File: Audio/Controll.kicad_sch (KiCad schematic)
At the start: 5 parts, among them K1 AZ850-x, K2 AZ850-x

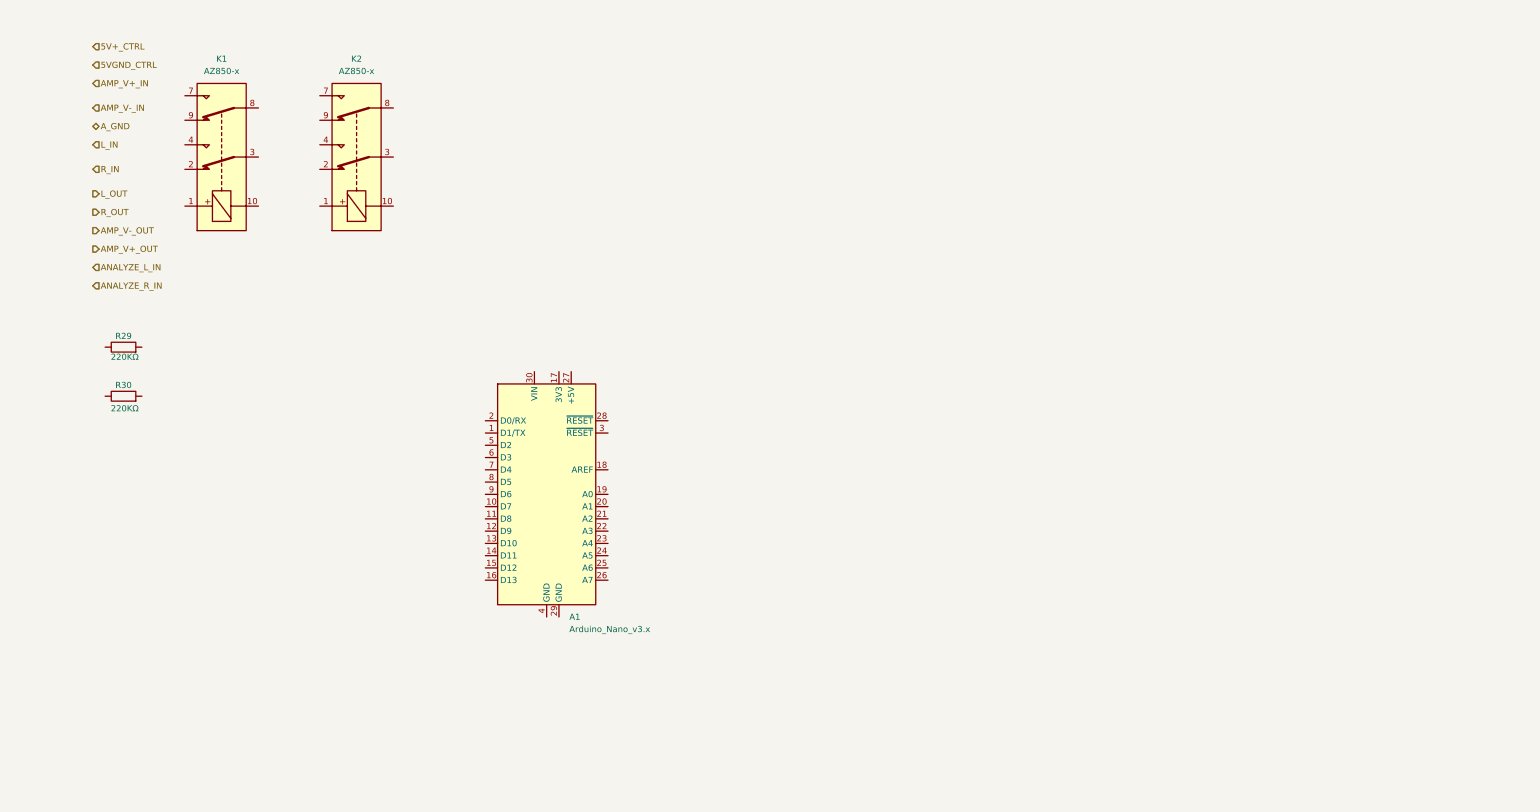
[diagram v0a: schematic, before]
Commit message: add relay
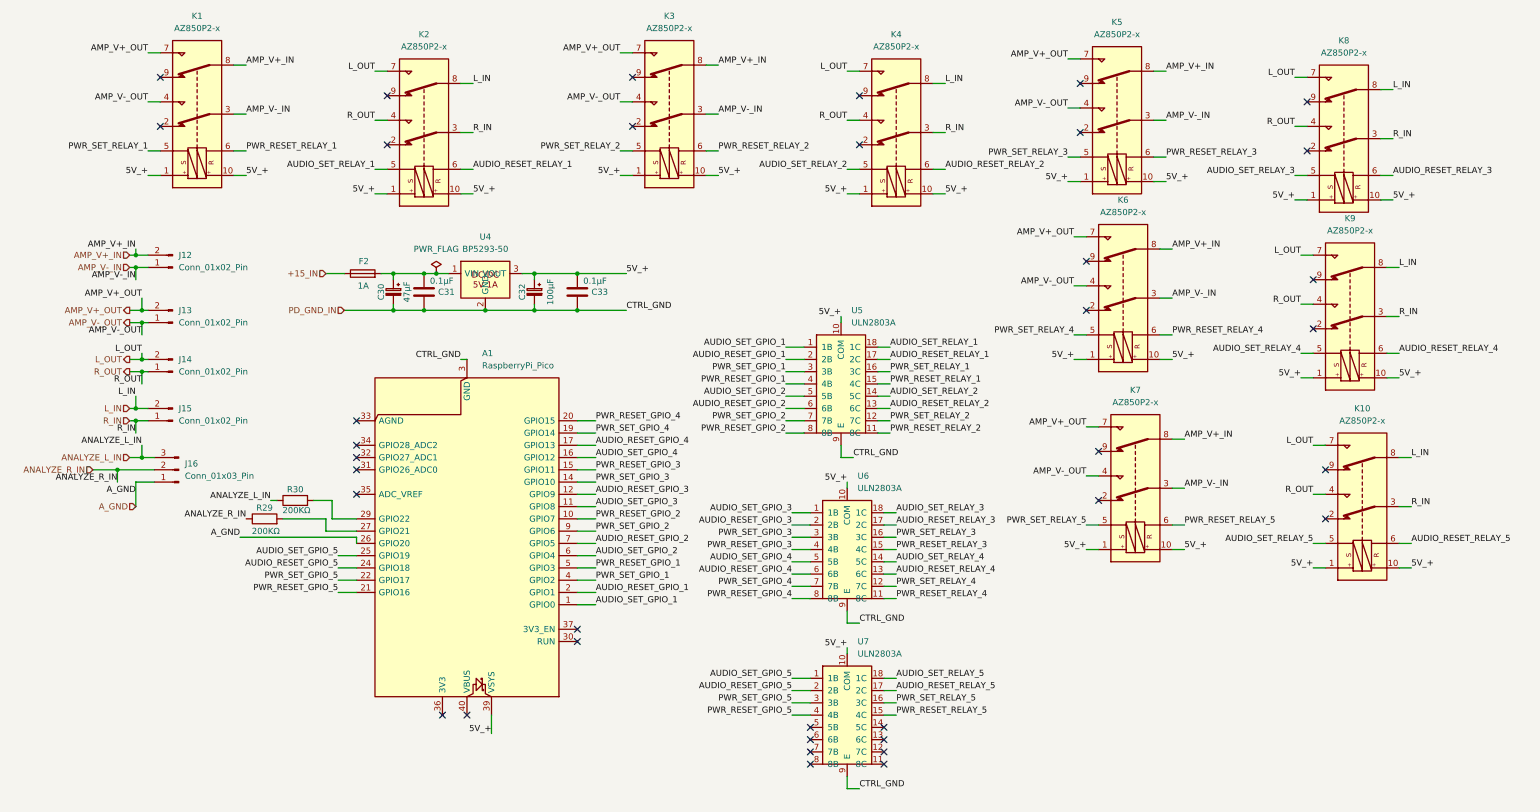
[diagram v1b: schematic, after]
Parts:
- removed A1: Arduino_Nano_v3.x, Module:Arduino_Nano, symbol MCU_Module:Arduino_Nano_v3.x
- removed K1, K2: AZ850-x, Relay_THT:Relay_DPDT_FRT5, symbol Relay:AZ850-x
- added A1: RaspberryPi_Pico, Module:RaspberryPi_Pico_Common_Unspecified, symbol MCU_Module:RaspberryPi_Pico
- added C30: 47μF, Capacitor_THT:CP_Radial_D8.0mm_P3.50mm, symbol Device:C_Polarized_Small
- added C31, C33: 0.1μF, Capacitor_THT:C_Disc_D5.0mm_W2.5mm_P2.50mm, symbol Device:C
- added C32: 100μF, Capacitor_THT:CP_Radial_D6.3mm_P2.50mm, symbol Device:C_Polarized_Small
- added F2: 1A, Resistor_THT:R_Axial_DIN0411_L9.9mm_D3.6mm_P12.70mm_Horizontal, symbol Device:Fuse
- added J12, J13, J14, J15: Conn_01x02_Pin, symbol Connector:Conn_01x02_Pin
- added J16: Conn_01x03_Pin, symbol Connector:Conn_01x03_Pin
- added K1, K10, K2, K3, K4, K5, K6, K7, K8, K9: AZ850P2-x, Relay_THT:Relay_DPDT_FRT5, symbol Relay:AZ850P2-x
- added U4: BP5293-50, BP5293_ROHM:BP5293-50_ROHM_SIP-3, symbol BP5293-50:BP5293-50
- added U5, U6, U7: ULN2803A, ULN2803A_HTC_DIP_ONLY:ULN2803A_DIP-18_W7.62mm, symbol ULN2803A:ULN2803A
- R29: renamed from R30; value 220KΩ -> 200KΩ
- R30: renamed from R29; value 220KΩ -> 200KΩ
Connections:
- net AMP_V+_IN: now also J12.2 (Pin_2), K1.8, K3.8, K5.8, K6.8, K7.8
- net AMP_V+_OUT: now also J13.2 (Pin_2), K1.7, K3.7, K5.7, K6.7, K7.7
- net AMP_V-_IN: now also J12.1 (Pin_1), K1.3, K3.3, K5.3, K6.3, K7.3
- net AMP_V-_OUT: now also J13.1 (Pin_1), K1.4, K3.4, K5.4, K6.4, K7.4
- net ANALYZE_L_IN: now also R30.1, J16.3 (Pin_3)
- net ANALYZE_R_IN: now also R29.1, J16.2 (Pin_2)
- net A_GND: now also A1.26 (GPIO20), J16.1 (Pin_1)
- net L_IN: now also J15.2 (Pin_2), K10.8, K2.8, K4.8, K8.8, K9.8
- net L_OUT: now also J14.2 (Pin_2), K10.7, K2.7, K4.7, K8.7, K9.7
- net R_IN: now also J15.1 (Pin_1), K10.3, K2.3, K4.3, K8.3, K9.3
- net R_OUT: now also J14.1 (Pin_1), K10.4, K2.4, K4.4, K8.4, K9.4
- net at R30.2: now also A1.29 (GPIO22)
- net at R29.2: now also A1.27 (GPIO21)
- new net: C30.1, C31.1, F2.2, U4.1 (VIN)
- new net +15_IN: F2.1
- new net 5V_+: A1.39 (VSYS), C32.1, C33.1, K1.1, K1.10, K10.1, K10.10, K2.1, K2.10, K3.1, K3.10, K4.1, K4.10, K5.1, K5.10, K6.1, K6.10, K7.1, K7.10, K8.1, K8.10, K9.1, K9.10, U4.3 (VOUT), U5.10 (COM), U6.10 (COM), U7.10 (COM)
- new net AUDIO_RESET_GPIO_1: A1.2 (GPIO1), U5.2 (2B)
- new net AUDIO_RESET_GPIO_2: A1.7 (GPIO5), U5.6 (6B)
- new net AUDIO_RESET_GPIO_3: A1.12 (GPIO9), U6.2 (2B)
- new net AUDIO_RESET_GPIO_4: A1.17 (GPIO13), U6.6 (6B)
- new net AUDIO_RESET_GPIO_5: A1.24 (GPIO18), U7.2 (2B)
- new net AUDIO_RESET_RELAY_1: K2.6, U5.17 (2C)
- new net AUDIO_RESET_RELAY_2: K4.6, U5.13 (6C)
- new net AUDIO_RESET_RELAY_3: K8.6, U6.17 (2C)
- new net AUDIO_RESET_RELAY_4: K9.6, U6.13 (6C)
- new net AUDIO_RESET_RELAY_5: K10.6, U7.17 (2C)
- new net AUDIO_SET_GPIO_1: A1.1 (GPIO0), U5.1 (1B)
- new net AUDIO_SET_GPIO_2: A1.6 (GPIO4), U5.5 (5B)
- new net AUDIO_SET_GPIO_3: A1.11 (GPIO8), U6.1 (1B)
- new net AUDIO_SET_GPIO_4: A1.16 (GPIO12), U6.5 (5B)
- new net AUDIO_SET_GPIO_5: A1.25 (GPIO19), U7.1 (1B)
- new net AUDIO_SET_RELAY_1: K2.5, U5.18 (1C)
- new net AUDIO_SET_RELAY_2: K4.5, U5.14 (5C)
- new net AUDIO_SET_RELAY_3: K8.5, U6.18 (1C)
- new net AUDIO_SET_RELAY_4: K9.5, U6.14 (5C)
- new net AUDIO_SET_RELAY_5: K10.5, U7.18 (1C)
- new net PD_GND_IN: A1.13 (GND), A1.18 (GND), A1.23 (GND), A1.28 (GND), A1.3 (GND), A1.38 (GND), A1.8 (GND), C30.2, C31.2, C32.2, C33.2, U4.2 (GND), U5.9 (E), U6.9 (E), U7.9 (E)
- new net PWR_RESET_GPIO_1: A1.5 (GPIO3), U5.4 (4B)
- new net PWR_RESET_GPIO_2: A1.10 (GPIO7), U5.8 (8B)
- new net PWR_RESET_GPIO_3: A1.15 (GPIO11), U6.4 (4B)
- new net PWR_RESET_GPIO_4: A1.20 (GPIO15), U6.8 (8B)
- new net PWR_RESET_GPIO_5: A1.21 (GPIO16), U7.4 (4B)
- new net PWR_RESET_RELAY_1: K1.6, U5.15 (4C)
- new net PWR_RESET_RELAY_2: K3.6, U5.11 (8C)
- new net PWR_RESET_RELAY_3: K5.6, U6.15 (4C)
- new net PWR_RESET_RELAY_4: K6.6, U6.11 (8C)
- new net PWR_RESET_RELAY_5: K7.6, U7.15 (4C)
- new net PWR_SET_GPIO_1: A1.4 (GPIO2), U5.3 (3B)
- new net PWR_SET_GPIO_2: A1.9 (GPIO6), U5.7 (7B)
- new net PWR_SET_GPIO_3: A1.14 (GPIO10), U6.3 (3B)
- new net PWR_SET_GPIO_4: A1.19 (GPIO14), U6.7 (7B)
- new net PWR_SET_GPIO_5: A1.22 (GPIO17), U7.3 (3B)
- new net PWR_SET_RELAY_1: K1.5, U5.16 (3C)
- new net PWR_SET_RELAY_2: K3.5, U5.12 (7C)
- new net PWR_SET_RELAY_3: K5.5, U6.16 (3C)
- new net PWR_SET_RELAY_4: K6.5, U6.12 (7C)
- new net PWR_SET_RELAY_5: K7.5, U7.16 (3C)
- no-connect marks 0 -> 37
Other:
- moved on the sheet: R29, R30

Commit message: remove analyze
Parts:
- removed J16: Conn_01x03_Pin, symbol Connector:Conn_01x03_Pin
- removed R29, R30: 200KΩ, Resistor_SMD:R_1206_3216Metric_Pad1.30x1.75mm_HandSolder, symbol Device:R
- added J17: Conn_01x02_Pin, symbol Connector:Conn_01x02_Pin
- added NT1: NetTie_2, symbol Device:NetTie_2
- U4: symbol BP5293-50:BP5293-50 -> BP5293_ROHM:BP5293-50
- U5, U6, U7: footprint ULN2803A_HTC_DIP_ONLY:ULN2803A_DIP-18_W7.62mm -> Library:ULN2803A_DIP-18_W7.62mm; symbol ULN2803A:ULN2803A -> Transistor_Array:ULN2803A
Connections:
- net +15_IN: now also J17.2 (Pin_2)
- net PD_GND_IN: now also J17.1 (Pin_1), NT1.1; no longer A1.13 (GND), A1.18 (GND), A1.23 (GND), A1.28 (GND), A1.3 (GND), A1.38 (GND), A1.8 (GND), C30.2, C31.2, C32.2, C33.2, U4.2 (GND), U5.9 (E), U6.9 (E), U7.9 (E)
- net A_GND: no longer names the net of A1.26 (GPIO20)
- new net CTRL_GND: A1.13 (GND), A1.18 (GND), A1.23 (GND), A1.28 (GND), A1.3 (GND), A1.38 (GND), A1.8 (GND), C30.2, C31.2, C32.2, C33.2, NT1.2, U4.2 (GND), U5.9 (GND), U6.9 (GND), U7.9 (GND)
- no-connect marks 37 -> 40

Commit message: connect gnd
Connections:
- net CTRL_GND: now also U7.5 (I5), U7.6 (I6), U7.7 (I7), U7.8 (I8)
- no-connect marks 40 -> 36
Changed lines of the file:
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@@
+	)
+	(junction
+		(at 162.56 168.91)
+		(diameter 0)
+		(color 0 0 0 0)
 	)
 	(junction
@@
 	)
 	(junction
+		(at 162.56 167.64)
+		(diameter 0)
+		(color 0 0 0 0)
+	)
+	(junction
 		(at 120.65 67.31)
 		(diameter 0)
@@
 	)
 	(junction
+		(at 162.56 166.37)
+		(diameter 0)
+		(color 0 0 0 0)
+	)
+	(junction
 		(at 27.94 128.27)
 		(diameter 0)
@@
 	)
 	(no_connect
-		(at 166.37 171.45)
-	)
-	(no_connect
 		(at 226.06 64.77)
 	)
@@
 	)
 	(no_connect
-		(at 166.37 166.37)
-	)
-	(no_connect
 		(at 273.05 68.58)
 	)
@@
 	)
 	(no_connect
-		(at 166.37 163.83)
-	)
-	(no_connect
 		(at 275.59 107.95)
 	)
@@
 	)
 	(no_connect
-		(at 166.37 168.91)
-	)
-	(no_connect
 		(at 275.59 118.11)
 	)
@@
 	(wire
 		(pts
+			(xy 166.37 168.91) (xy 162.56 168.91)
+		)
+		(stroke
+			(width 0)
+			(type default)
+		)
+	)
+	(wire
+		(pts
 			(xy 49.53 41.91) (xy 52.07 41.91)
 		)
@@
 	(wire
 		(pts
+			(xy 162.56 163.83) (xy 162.56 166.37)
+		)
+		(stroke
+			(width 0)
+			(type default)
+		)
+	)
+	(wire
+		(pts
 			(xy 176.53 25.4) (xy 179.07 25.4)
 		)
@@
 	(wire
 		(pts
+			(xy 162.56 166.37) (xy 162.56 167.64)
+		)
+		(stroke
+			(width 0)
+			(type default)
+		)
+	)
+	(wire
+		(pts
 			(xy 82.55 74.93) (xy 82.55 73.66)
 		)
@@
 	(wire
 		(pts
+			(xy 166.37 171.45) (xy 162.56 171.45)
+		)
+		(stroke
+			(width 0)
+			(type default)
+		)
+	)
+	(wire
+		(pts
 			(xy 49.53 34.29) (xy 52.07 34.29)
 		)
@@
 	(wire
 		(pts
+			(xy 162.56 167.64) (xy 162.56 168.91)
+		)
+		(stroke
+			(width 0)
+			(type default)
+		)
+	)
+	(wire
+		(pts
 			(xy 147.32 41.91) (xy 149.86 41.91)
 		)
@@
 	(wire
 		(pts
+			(xy 166.37 163.83) (xy 162.56 163.83)
+		)
+		(stroke
+			(width 0)
+			(type default)
+		)
+	)
+	(wire
+		(pts
 			(xy 120.65 105.41) (xy 124.46 105.41)
 		)
@@
 	(wire
 		(pts
+			(xy 166.37 166.37) (xy 162.56 166.37)
+		)
+		(stroke
+			(width 0)
+			(type default)
+		)
+	)
+	(wire
+		(pts
+			(xy 162.56 171.45) (xy 162.56 168.91)
+		)
+		(stroke
+			(width 0)
+			(type default)
+		)
+	)
+	(wire
+		(pts
 			(xy 194.31 45.72) (xy 196.85 45.72)
 		)
@@
 		(pts
 			(xy 78.74 45.72) (xy 81.28 45.72)
+		)
+		(stroke
+			(width 0)
+			(type default)
+		)
+	)
+	(wire
+		(pts
+			(xy 158.75 167.64) (xy 162.56 167.64)
 		)
 		(stroke
@@
 		)
 	)
+	(label "CTRL_GND"
+		(at 158.75 167.64 180)
+		(effects
+			(font
+				(size 1.27 1.27)
+			)
+			(justify right bottom)
+		)
+	)
